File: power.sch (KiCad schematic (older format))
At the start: 21 parts, among them J2 Conn_01x02_Male, U4 PAM2401, U5 MCP73831-2-OT

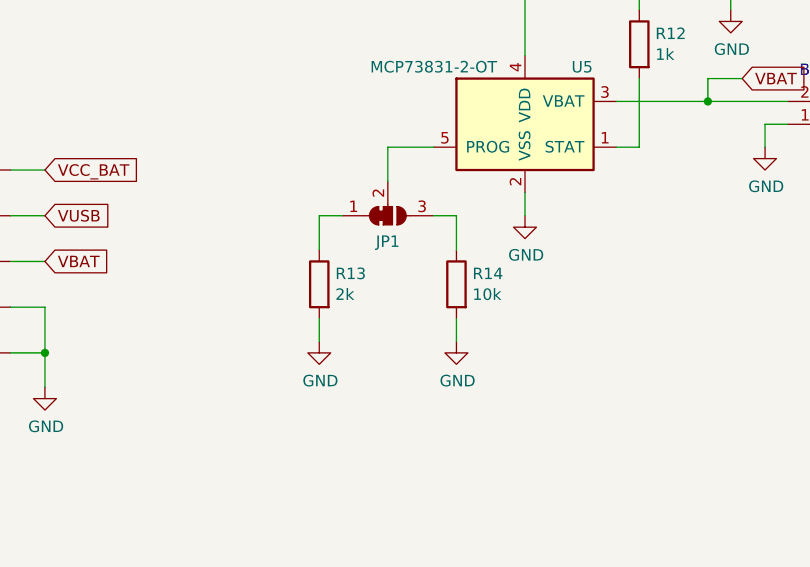
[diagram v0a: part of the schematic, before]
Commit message: Route switches
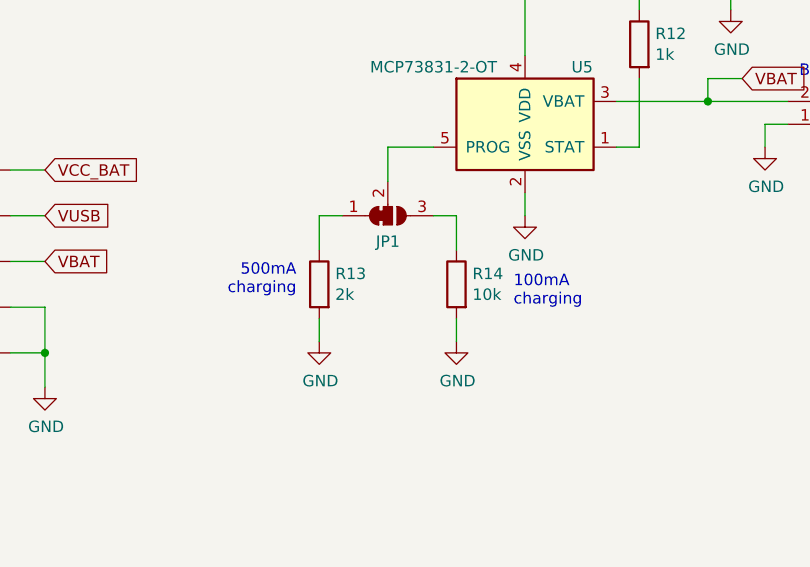
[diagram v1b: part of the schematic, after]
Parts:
- JP1: footprint Connector_PinHeader_2.54mm:PinHeader_1x03_P2.54mm_Vertical -> Jumper:SolderJumper-3_P1.3mm_Bridged2Bar12_Pad1.0x1.5mm
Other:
- note added: "100mA\ncharging\n"
- note added: "500mA\ncharging"
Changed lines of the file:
@@
 F 0 "JP1" H 4650 2763 50  0000 C CNN
 F 1 "SolderJumper_3_Bridged12" H 4650 2854 50  0001 C CNN
-F 2 "Connector_PinHeader_2.54mm:PinHeader_1x03_P2.54mm_Vertical" H 4650 2650 50  0001 C CNN
+F 2 "Jumper:SolderJumper-3_P1.3mm_Bridged2Bar12_Pad1.0x1.5mm" H 4650 2650 50  0001 C CNN
 F 3 "~" H 4650 2650 50  0001 C CNN
 	1    4650 2650
@@
 	1    0    0    -1
 $EndComp
+Text Notes 4250 3000 2    50   ~ 0
+500mA\ncharging
+Text Notes 5200 3050 0    50   ~ 0
+100mA\ncharging\n
 $EndSCHEMATC

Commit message: Wire ISP/USB to debug headers
Change L1 footprint
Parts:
- L1: footprint Inductor_SMD:L_Vishay_IHLP-1212 -> Inductor_SMD:L_Taiyo-Yuden_NR-50xx_HandSoldering
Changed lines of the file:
@@
 F 0 "L1" V 2840 4650 50  0000 C CNN
 F 1 "2.2u 3A" V 2749 4650 50  0000 C CNN
-F 2 "Inductor_SMD:L_Vishay_IHLP-1212" H 2650 4650 50  0001 C CNN
+F 2 "Inductor_SMD:L_Taiyo-Yuden_NR-50xx_HandSoldering" H 2650 4650 50  0001 C CNN
 F 3 "~" H 2650 4650 50  0001 C CNN
 	1    2650 4650
